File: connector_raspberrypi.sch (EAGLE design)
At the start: 1 part, among them J1 RASPBERRYPI-40-PIN-GPIO_PTH_N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

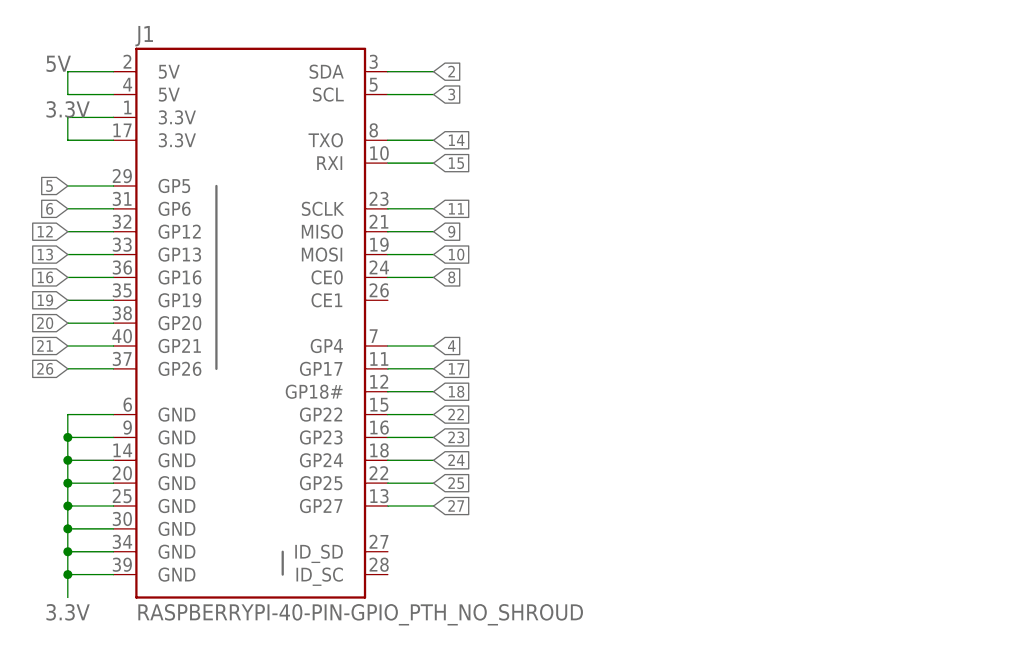
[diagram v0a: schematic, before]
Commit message: Fix connector poss, Added -i option for json input as arg, added pyPath to get folder path
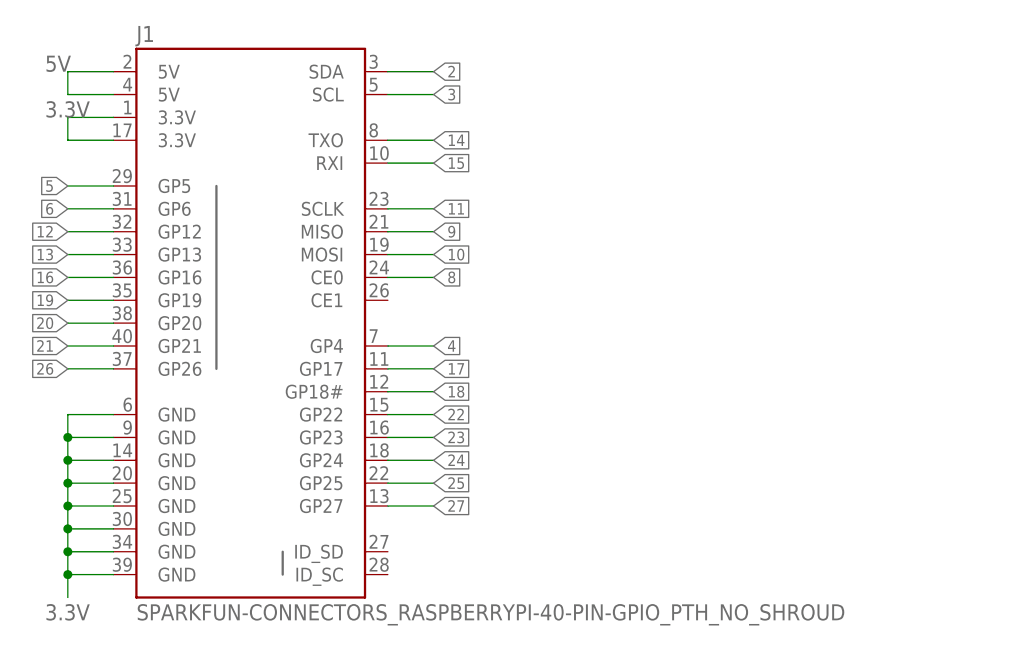
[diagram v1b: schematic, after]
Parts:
- J1: value RASPBERRYPI-40-PIN-GPIO_PTH_NO_SHROUD -> SPARKFUN-CONNECTORS_RASPBERRYPI-40-PIN-GPIO_PTH_NO_SHROUD; device SparkFun-Connectors:RASPBERRYPI-40-PIN-GPIO_PTH_NO_SHROUD -> connector_raspberrypi:SPARKFUN-CONNECTORS_RASPBERRYPI-40-PIN-GPIO_PTH_NO_SHROUD
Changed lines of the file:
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@@
 <settings>
 <setting alwaysvectorfont="no"/>
+<setting keepoldvectorfont="yes"/>
 <setting verticaltext="up"/>
 </settings>
@@
 </classes>
 <parts>
-<part name="J1" library="SparkFun-Connectors" deviceset="RASPBERRYPI-40-PIN-GPIO" device="_PTH_NO_SHROUD"/>
+<part name="J1" library="connector_raspberrypi" deviceset="SPARKFUN-CONNECTORS_RASPBERRYPI-40-PIN-GPIO" device="_PTH_NO_SHROUD"/>
 </parts>
 <sheets>

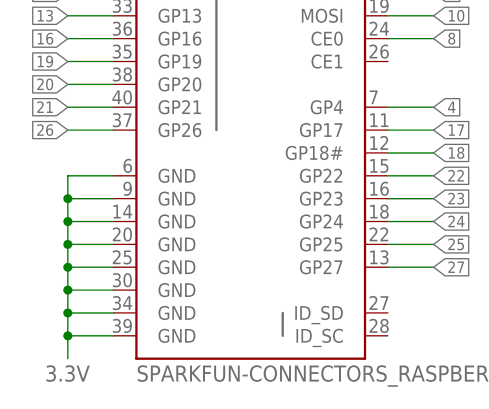
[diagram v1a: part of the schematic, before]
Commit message: Adding board boarders and required CAM files
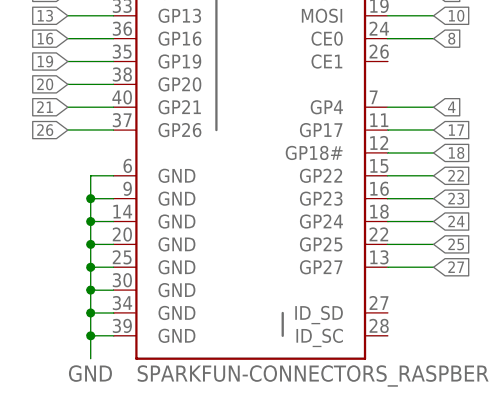
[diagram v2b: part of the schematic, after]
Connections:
- new net GND: J1.GND@14, J1.GND@20, J1.GND@25, J1.GND@30, J1.GND@34, J1.GND@39, J1.GND@6, J1.GND@9
- net 3.3V: no longer J1.GND@14, J1.GND@20, J1.GND@25, J1.GND@30, J1.GND@34, J1.GND@39, J1.GND@6, J1.GND@9
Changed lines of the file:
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@@
 <label x="-25.4" y="17.78" size="1.778" layer="95"/>
 </segment>
+</net>
+<net name="GND" class="0">
 <segment>
+<pinref part="J1" gate="G$1" pin="GND@6"/>
+<wire x1="-17.78" y1="-15.24" x2="-20.32" y2="-15.24" width="0.1524" layer="91"/>
+<wire x1="-20.32" y1="-15.24" x2="-20.32" y2="-17.78" width="0.1524" layer="91"/>
+<pinref part="J1" gate="G$1" pin="GND@9"/>
+<wire x1="-20.32" y1="-17.78" x2="-20.32" y2="-20.32" width="0.1524" layer="91"/>
+<wire x1="-20.32" y1="-20.32" x2="-20.32" y2="-22.86" width="0.1524" layer="91"/>
+<wire x1="-20.32" y1="-22.86" x2="-20.32" y2="-25.4" width="0.1524" layer="91"/>
+<wire x1="-20.32" y1="-25.4" x2="-20.32" y2="-27.94" width="0.1524" layer="91"/>
+<wire x1="-20.32" y1="-27.94" x2="-20.32" y2="-30.48" width="0.1524" layer="91"/>
+<wire x1="-20.32" y1="-30.48" x2="-20.32" y2="-33.02" width="0.1524" layer="91"/>
+<wire x1="-20.32" y1="-33.02" x2="-20.32" y2="-35.56" width="0.1524" layer="91"/>
+<wire x1="-17.78" y1="-17.78" x2="-20.32" y2="-17.78" width="0.1524" layer="91"/>
+<junction x="-20.32" y="-17.78"/>
+<pinref part="J1" gate="G$1" pin="GND@14"/>
+<wire x1="-17.78" y1="-20.32" x2="-20.32" y2="-20.32" width="0.1524" layer="91"/>
+<junction x="-20.32" y="-20.32"/>
+<pinref part="J1" gate="G$1" pin="GND@20"/>
+<wire x1="-17.78" y1="-22.86" x2="-20.32" y2="-22.86" width="0.1524" layer="91"/>
+<junction x="-20.32" y="-22.86"/>
+<pinref part="J1" gate="G$1" pin="GND@25"/>
+<wire x1="-17.78" y1="-25.4" x2="-20.32" y2="-25.4" width="0.1524" layer="91"/>
+<junction x="-20.32" y="-25.4"/>
+<pinref part="J1" gate="G$1" pin="GND@30"/>
+<wire x1="-17.78" y1="-27.94" x2="-20.32" y2="-27.94" width="0.1524" layer="91"/>
+<junction x="-20.32" y="-27.94"/>
+<pinref part="J1" gate="G$1" pin="GND@34"/>
+<wire x1="-17.78" y1="-30.48" x2="-20.32" y2="-30.48" width="0.1524" layer="91"/>
+<junction x="-20.32" y="-30.48"/>
 <pinref part="J1" gate="G$1" pin="GND@39"/>
-<wire x1="-17.78" y1="-33.02" x2="-22.86" y2="-33.02" width="0.1524" layer="91"/>
-<wire x1="-22.86" y1="-33.02" x2="-22.86" y2="-35.56" width="0.1524" layer="91"/>
-<pinref part="J1" gate="G$1" pin="GND@34"/>
-<wire x1="-17.78" y1="-30.48" x2="-22.86" y2="-30.48" width="0.1524" layer="91"/>
-<wire x1="-22.86" y1="-30.48" x2="-22.86" y2="-33.02" width="0.1524" layer="91"/>
-<junction x="-22.86" y="-33.02"/>
-<pinref part="J1" gate="G$1" pin="GND@30"/>
-<wire x1="-17.78" y1="-27.94" x2="-22.86" y2="-27.94" width="0.1524" layer="91"/>
-<wire x1="-22.86" y1="-27.94" x2="-22.86" y2="-30.48" width="0.1524" layer="91"/>
-<junction x="-22.86" y="-30.48"/>
-<pinref part="J1" gate="G$1" pin="GND@25"/>
-<wire x1="-17.78" y1="-25.4" x2="-22.86" y2="-25.4" width="0.1524" layer="91"/>
-<wire x1="-22.86" y1="-25.4" x2="-22.86" y2="-27.94" width="0.1524" layer="91"/>
-<junction x="-22.86" y="-27.94"/>
-<pinref part="J1" gate="G$1" pin="GND@20"/>
-<wire x1="-17.78" y1="-22.86" x2="-22.86" y2="-22.86" width="0.1524" layer="91"/>
-<wire x1="-22.86" y1="-22.86" x2="-22.86" y2="-25.4" width="0.1524" layer="91"/>
-<junction x="-22.86" y="-25.4"/>
-<pinref part="J1" gate="G$1" pin="GND@14"/>
-<wire x1="-17.78" y1="-20.32" x2="-22.86" y2="-20.32" width="0.1524" layer="91"/>
-<wire x1="-22.86" y1="-20.32" x2="-22.86" y2="-22.86" width="0.1524" layer="91"/>
-<junction x="-22.86" y="-22.86"/>
-<pinref part="J1" gate="G$1" pin="GND@9"/>
-<wire x1="-17.78" y1="-17.78" x2="-22.86" y2="-17.78" width="0.1524" layer="91"/>
-<wire x1="-22.86" y1="-17.78" x2="-22.86" y2="-20.32" width="0.1524" layer="91"/>
-<junction x="-22.86" y="-20.32"/>
-<pinref part="J1" gate="G$1" pin="GND@6"/>
-<wire x1="-17.78" y1="-15.24" x2="-22.86" y2="-15.24" width="0.1524" layer="91"/>
-<wire x1="-22.86" y1="-15.24" x2="-22.86" y2="-17.78" width="0.1524" layer="91"/>
-<junction x="-22.86" y="-17.78"/>
-<label x="-25.4" y="-38.1" size="1.778" layer="95"/>
+<wire x1="-17.78" y1="-33.02" x2="-20.32" y2="-33.02" width="0.1524" layer="91"/>
+<junction x="-20.32" y="-33.02"/>
+<label x="-22.86" y="-38.1" size="1.778" layer="95"/>
 </segment>
 </net>
